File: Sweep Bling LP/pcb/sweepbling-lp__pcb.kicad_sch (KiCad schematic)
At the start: 46 parts, among them SW1 SW_Push, SW10 SW_Push, SW10_r1 SW_Push, SW11 SW_Push, SW11_r1 SW_Push, SW12 SW_Push, SW12_r1 SW_Push, SW13 SW_Push, SW13_r1 SW_Push, SW14 SW_Push, SW14_r1 SW_Push, SW15 SW_Push, SW15_r1 SW_Push, SW16 SW_Push, SW16_r1 SW_Push, SW17 SW_Push, SW17_r1 SW_Push, SW1_r1 SW_Push, SW2 SW_Push, SW2_r1 SW_Push, SW3 SW_Push, SW3_r1 SW_Push, SW4 SW_Push, SW4_r1 SW_Push, SW5 SW_Push, SW5_r1 SW_Push, SW6 SW_Push, SW6_r1 SW_Push, SW7 SW_Push, SW7_r1 SW_Push, SW8 SW_Push, SW8_r1 SW_Push, SW9 SW_Push, SW9_r1 SW_Push, U1 ProMicro-kbd, U2 ProMicro-kbd

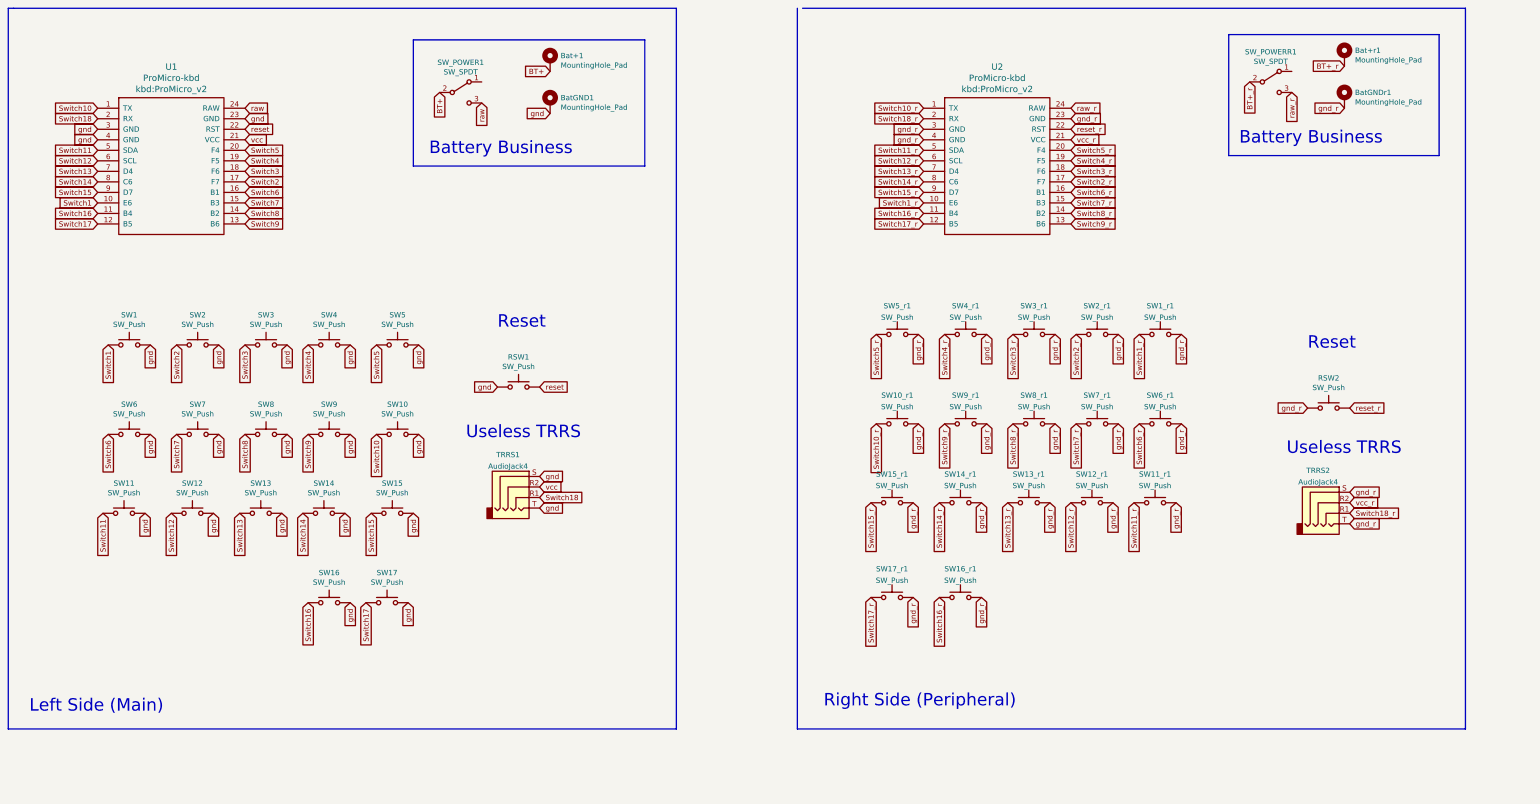
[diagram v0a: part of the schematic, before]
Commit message: edited Blink_LP
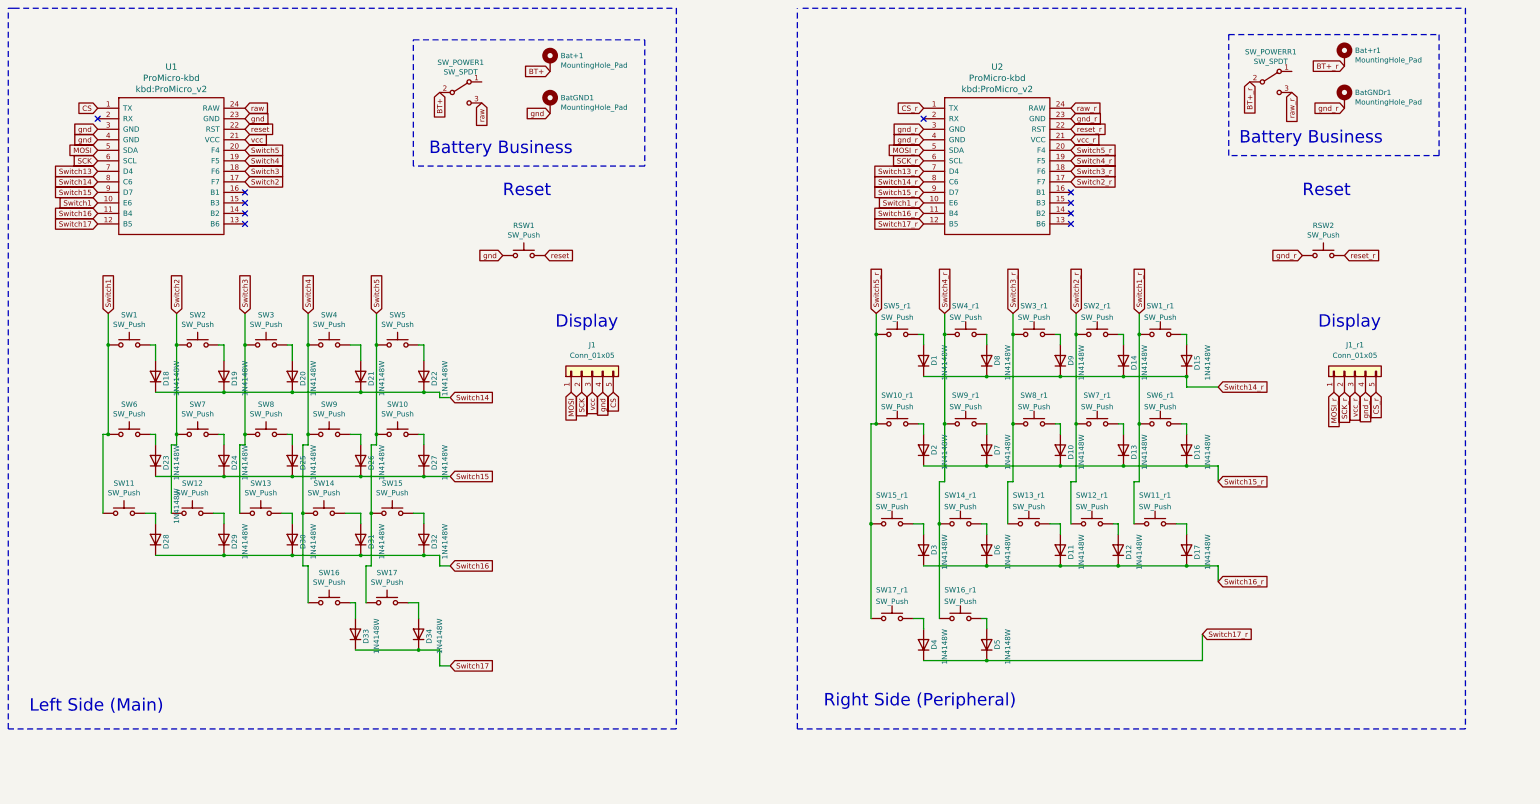
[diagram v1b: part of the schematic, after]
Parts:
- removed TRRS1, TRRS2: AudioJack4, symbol Connector:AudioJack4
- added D1, D10, D11, D12, D13, D14, D15, D16, D17, D18, D19, D2, D20, D21, D22, D23, D24, D25, D26, D27, D28, D29, D3, D30, D31, D32, D33, D34, D4, D5, D6, D7, D8, D9: 1N4148W, Diode_SMD:D_SOD-123, symbol Diode:1N4148W
- added J1, J1_r1: Conn_01x05, Connector_PinSocket_2.54mm:PinSocket_1x05_P2.54mm_Vertical, symbol Connector_Generic:Conn_01x05
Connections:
- net Switch1: now also SW11.1, SW6.1
- net Switch13: no longer SW13.1
- net Switch13_r: no longer SW13_r1.1
- net Switch14: now also D18.1 (K), D19.1 (K), D20.1 (K), D21.1 (K), D22.1 (K); no longer SW14.1
- net Switch14_r: now also D1.1 (K), D14.1 (K), D15.1 (K), D8.1 (K), D9.1 (K); no longer SW14_r1.1
- net Switch15: now also D23.1 (K), D24.1 (K), D25.1 (K), D26.1 (K), D27.1 (K); no longer SW15.1
- net Switch15_r: now also D10.1 (K), D13.1 (K), D16.1 (K), D2.1 (K), D7.1 (K); no longer SW15_r1.1
- net Switch16: now also D28.1 (K), D29.1 (K), D30.1 (K), D31.1 (K), D32.1 (K); no longer SW16.1
- net Switch16_r: now also D11.1 (K), D12.1 (K), D17.1 (K), D3.1 (K), D6.1 (K); no longer SW16_r1.1
- net Switch17: now also D33.1 (K), D34.1 (K); no longer SW17.1
- net Switch17_r: now also D4.1 (K), D5.1 (K); no longer SW17_r1.1
- net Switch1_r: now also SW11_r1.1, SW6_r1.1
- net Switch2: now also SW12.1, SW7.1
- net Switch2_r: now also SW12_r1.1, SW7_r1.1
- net Switch3: now also SW13.1, SW8.1
- net Switch3_r: now also SW13_r1.1, SW8_r1.1
- net Switch4: now also SW14.1, SW16.1, SW9.1
- net Switch4_r: now also SW14_r1.1, SW16_r1.1, SW9_r1.1
- net Switch5: now also SW10.1, SW15.1, SW17.1
- net Switch5_r: now also SW10_r1.1, SW15_r1.1, SW17_r1.1
- net gnd: now also J1.4 (Pin_4); no longer SW1.2, SW10.2, SW11.2, SW12.2, SW13.2, SW14.2, SW15.2, SW16.2, SW17.2, SW2.2, SW3.2, SW4.2, SW5.2, SW6.2, SW7.2, SW8.2, SW9.2
- net gnd_r: now also J1_r1.4 (Pin_4); no longer SW10_r1.2, SW11_r1.2, SW12_r1.2, SW13_r1.2, SW14_r1.2, SW15_r1.2, SW16_r1.2, SW17_r1.2, SW1_r1.2, SW2_r1.2, SW3_r1.2, SW4_r1.2, SW5_r1.2, SW6_r1.2, SW7_r1.2, SW8_r1.2, SW9_r1.2
- net vcc: now also J1.3 (Pin_3)
- net vcc_r: now also J1_r1.3 (Pin_3)
- net Switch10 renamed CS
- net CS: now also J1.5 (Pin_5); no longer SW10.1
- net Switch10_r renamed CS_r
- net CS_r: now also J1_r1.5 (Pin_5); no longer SW10_r1.1
- net Switch11 renamed MOSI
- net MOSI: now also J1.1 (Pin_1); no longer SW11.1
- net Switch11_r renamed MOSI_r
- net MOSI_r: now also J1_r1.1 (Pin_1); no longer SW11_r1.1
- net Switch12 renamed SCK
- net SCK: now also J1.2 (Pin_2); no longer SW12.1
- net Switch12_r renamed SCK_r
- net SCK_r: now also J1_r1.2 (Pin_2); no longer SW12_r1.1
- net Switch18: no longer names the net of U1.2 (RX)
- net Switch18_r: no longer names the net of U2.2 (RX)
- net Switch6: no longer names the net of U1.16 (B1)
- net Switch6: no longer SW6.1
- net Switch6_r: no longer names the net of U2.16 (B1)
- net Switch6_r: no longer SW6_r1.1
- net Switch7: no longer names the net of U1.15 (B3)
- net Switch7: no longer SW7.1
- net Switch7_r: no longer names the net of U2.15 (B3)
- net Switch7_r: no longer SW7_r1.1
- net Switch8: no longer names the net of U1.14 (B2)
- net Switch8: no longer SW8.1
- net Switch8_r: no longer names the net of U2.14 (B2)
- net Switch8_r: no longer SW8_r1.1
- net Switch9: no longer names the net of U1.13 (B6)
- net Switch9: no longer SW9.1
- net Switch9_r: no longer names the net of U2.13 (B6)
- net Switch9_r: no longer SW9_r1.1
- new net: D18.2 (A), SW1.2
- new net: D19.2 (A), SW2.2
- new net: D20.2 (A), SW3.2
- new net: D21.2 (A), SW4.2
- new net: D22.2 (A), SW5.2
- new net: D33.2 (A), SW16.2
- new net: D34.2 (A), SW17.2
- new net: D23.2 (A), SW6.2
- new net: D24.2 (A), SW7.2
- new net: D25.2 (A), SW8.2
- new net: D26.2 (A), SW9.2
- new net: D27.2 (A), SW10.2
- new net: D28.2 (A), SW11.2
- new net: D29.2 (A), SW12.2
- new net: D30.2 (A), SW13.2
- new net: D31.2 (A), SW14.2
- new net: D32.2 (A), SW15.2
- new net: D15.2 (A), SW1_r1.2
- new net: D14.2 (A), SW2_r1.2
- new net: D9.2 (A), SW3_r1.2
- new net: D8.2 (A), SW4_r1.2
- new net: D1.2 (A), SW5_r1.2
- new net: D5.2 (A), SW16_r1.2
- new net: D4.2 (A), SW17_r1.2
- new net: D16.2 (A), SW6_r1.2
- new net: D13.2 (A), SW7_r1.2
- new net: D10.2 (A), SW8_r1.2
- new net: D7.2 (A), SW9_r1.2
- new net: D2.2 (A), SW10_r1.2
- new net: D17.2 (A), SW11_r1.2
- new net: D12.2 (A), SW12_r1.2
- new net: D11.2 (A), SW13_r1.2
- new net: D6.2 (A), SW14_r1.2
- new net: D3.2 (A), SW15_r1.2
- no-connect marks 0 -> 10
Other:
- note added: "Display"
- note removed: "Useless TRRS"
- moved on the sheet: RSW1, RSW2, SW11_r1, SW12_r1, SW13_r1, SW14_r1, SW15_r1, SW16_r1, SW17_r1
